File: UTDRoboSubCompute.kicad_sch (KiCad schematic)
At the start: 56 parts, among them IC1 TPD4E05U06QDQARQ1, IC2 TPD4E05U06QDQARQ1, J1 Disable Bluetooth/Wifi, J10 HEADER-3X04, J11 HEADER-3X04, J12 HEADER-3X04, J13 Conn_02x20_Odd_Even, J14 GSB3116344KHHR, J15 GSB3116344KHHR, J16 TF38-22S-0.5SV_830_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

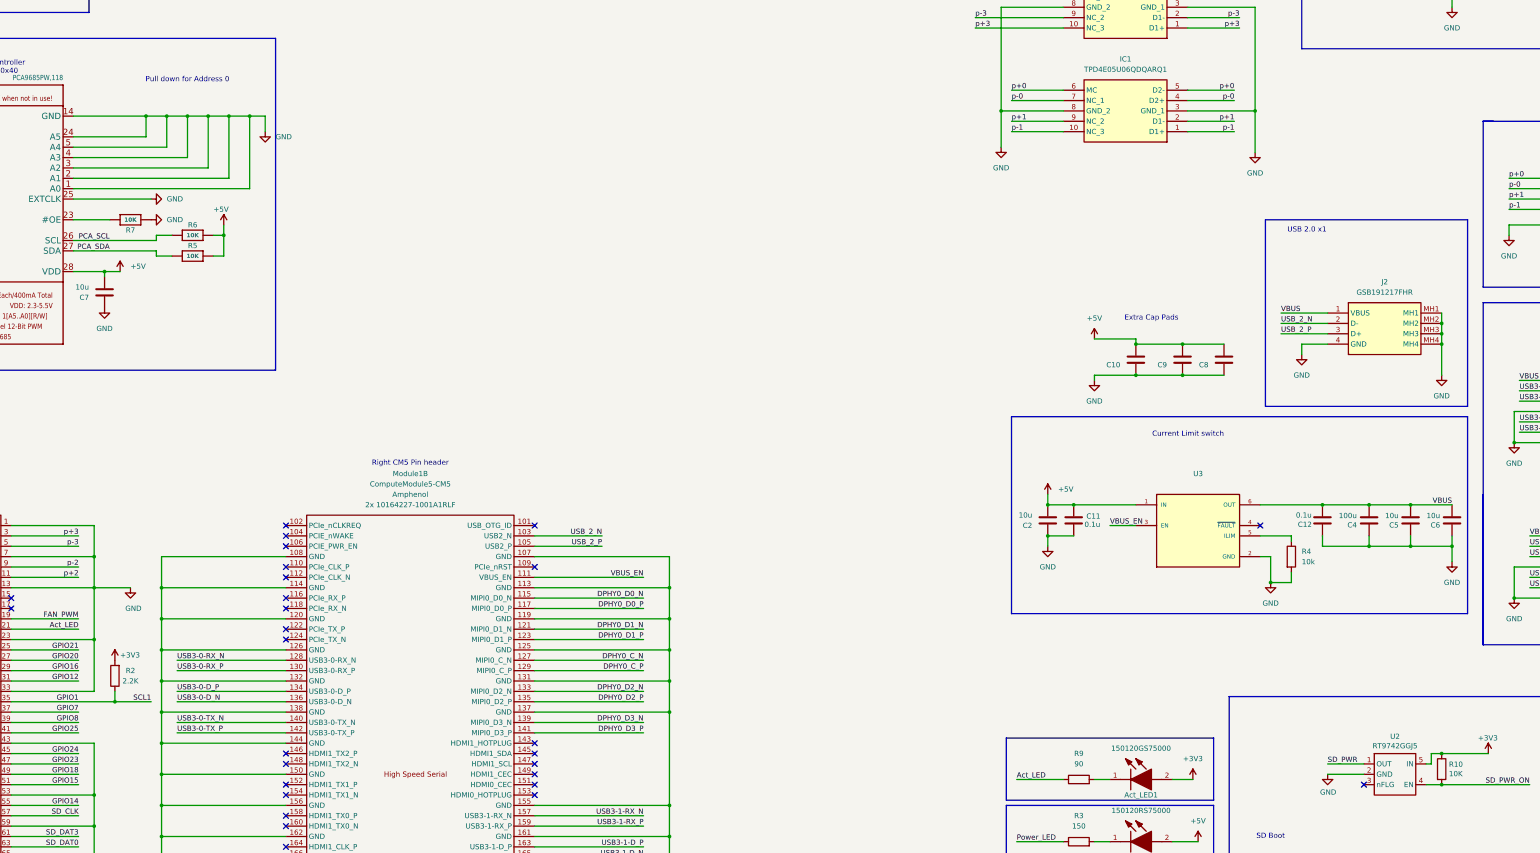
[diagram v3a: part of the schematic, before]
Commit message: Removed unneeded pull down
Removed unnecessary pull down resistor on the OE pin of the Servo Controller. Since I am not folding out the output enable pin, a pull down is not needed
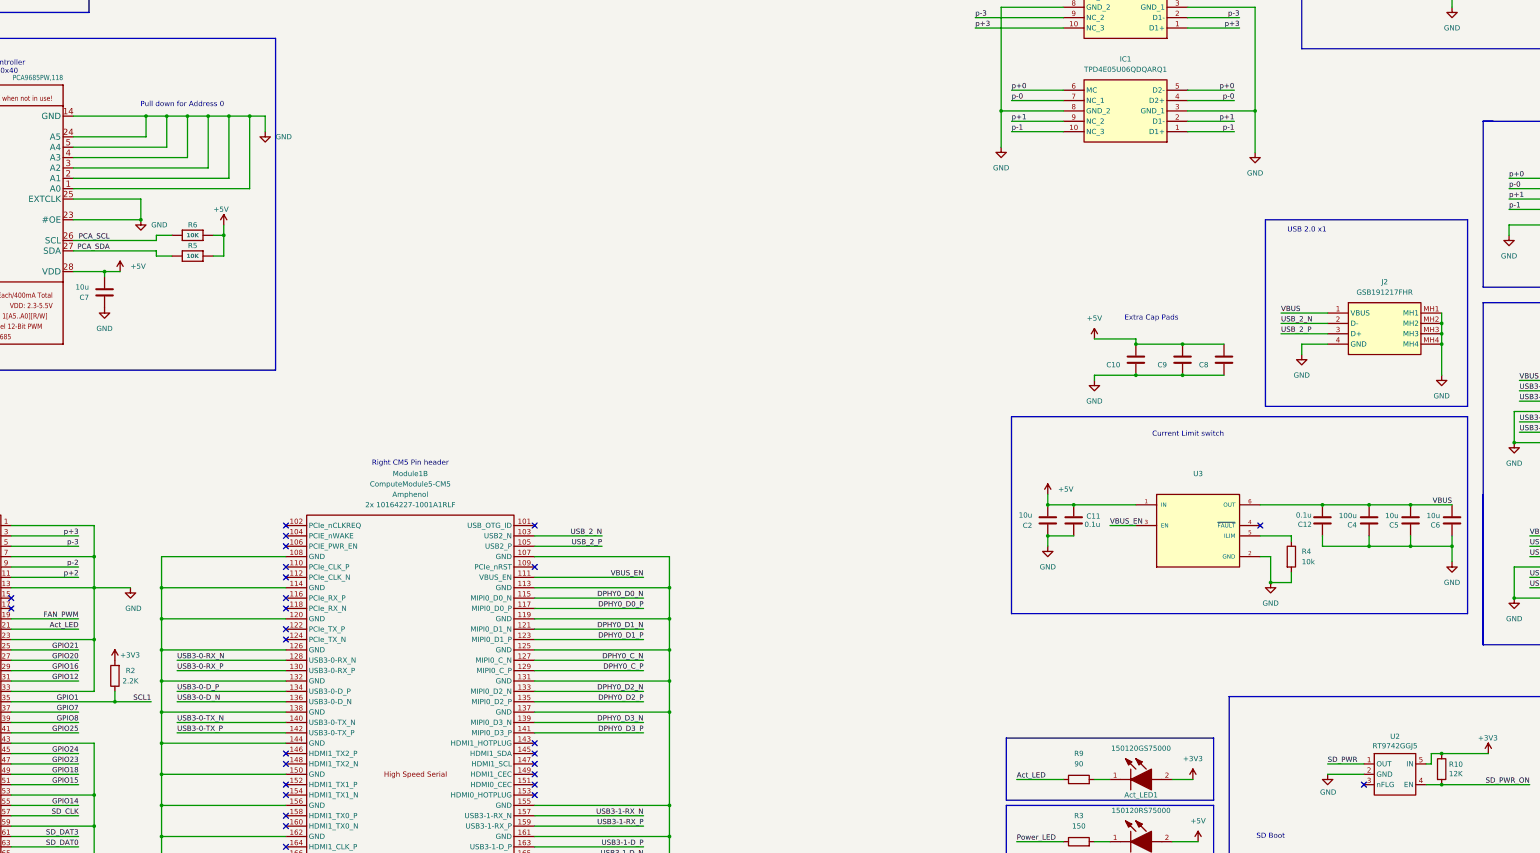
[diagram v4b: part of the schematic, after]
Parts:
- removed R7: 10K, Resistor_SMD:R_0805_2012Metric_Pad1.20x1.40mm_HandSolder, symbol Adafruit PCA9685 rev C-eagle-import:RESISTOR0805_NOOUTLINE
- R10: value 10K -> 12K; Field4 Farnell -> (none); Field6 MCR01MZPF1002 -> RP0805FRE0712KL; Field7 Rohm -> YAGEO; Mouser Part Number 667-ERJ-UP6D1002V -> 603-RP0805FRE0712KL
- U2: Field5 2545875 -> 2545875
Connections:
- net GND: now also U4.23 (#OE)

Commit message: Finished first verson
- updated bom
- added a more caps
- changed value of resistor according to data sheet
- updated ibom
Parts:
- renumbered Act_LED1 to Act1, Pwr_Led1 to Pwr1
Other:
- moved on the sheet: R1, R8
